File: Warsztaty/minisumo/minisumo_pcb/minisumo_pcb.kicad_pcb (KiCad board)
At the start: 2 copper layers, 100 x 100 mm, 49 parts, among them J1 HTSW-102-08-L-S, Q1 PMOS, U1 SN74LVC2G14DBV, U10 ITR8307-S17-TR8, U11 ITR8307-S17-TR8, U14 TB6612FNG, U2 TB6612FNG, U4 ATMEGA328P-AU, U7 LM1117S-5.0, U8 ITR8307-S17-TR8, Y1 ECS-160-20-4DN

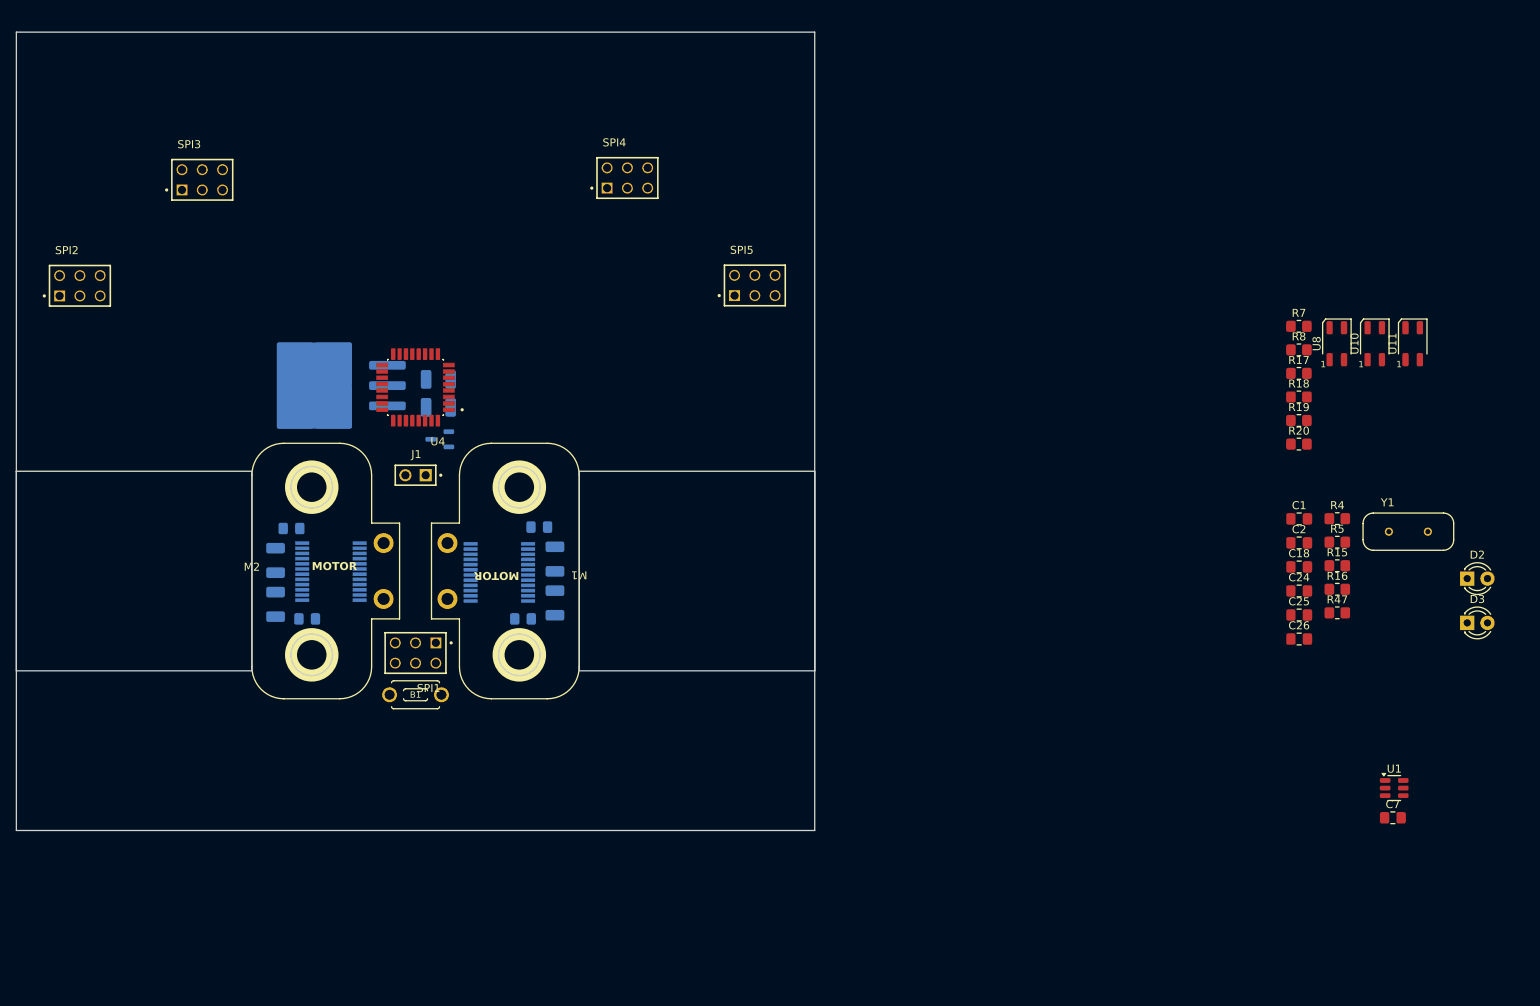
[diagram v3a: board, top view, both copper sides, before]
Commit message: Wstępny wyglad robota i płytki
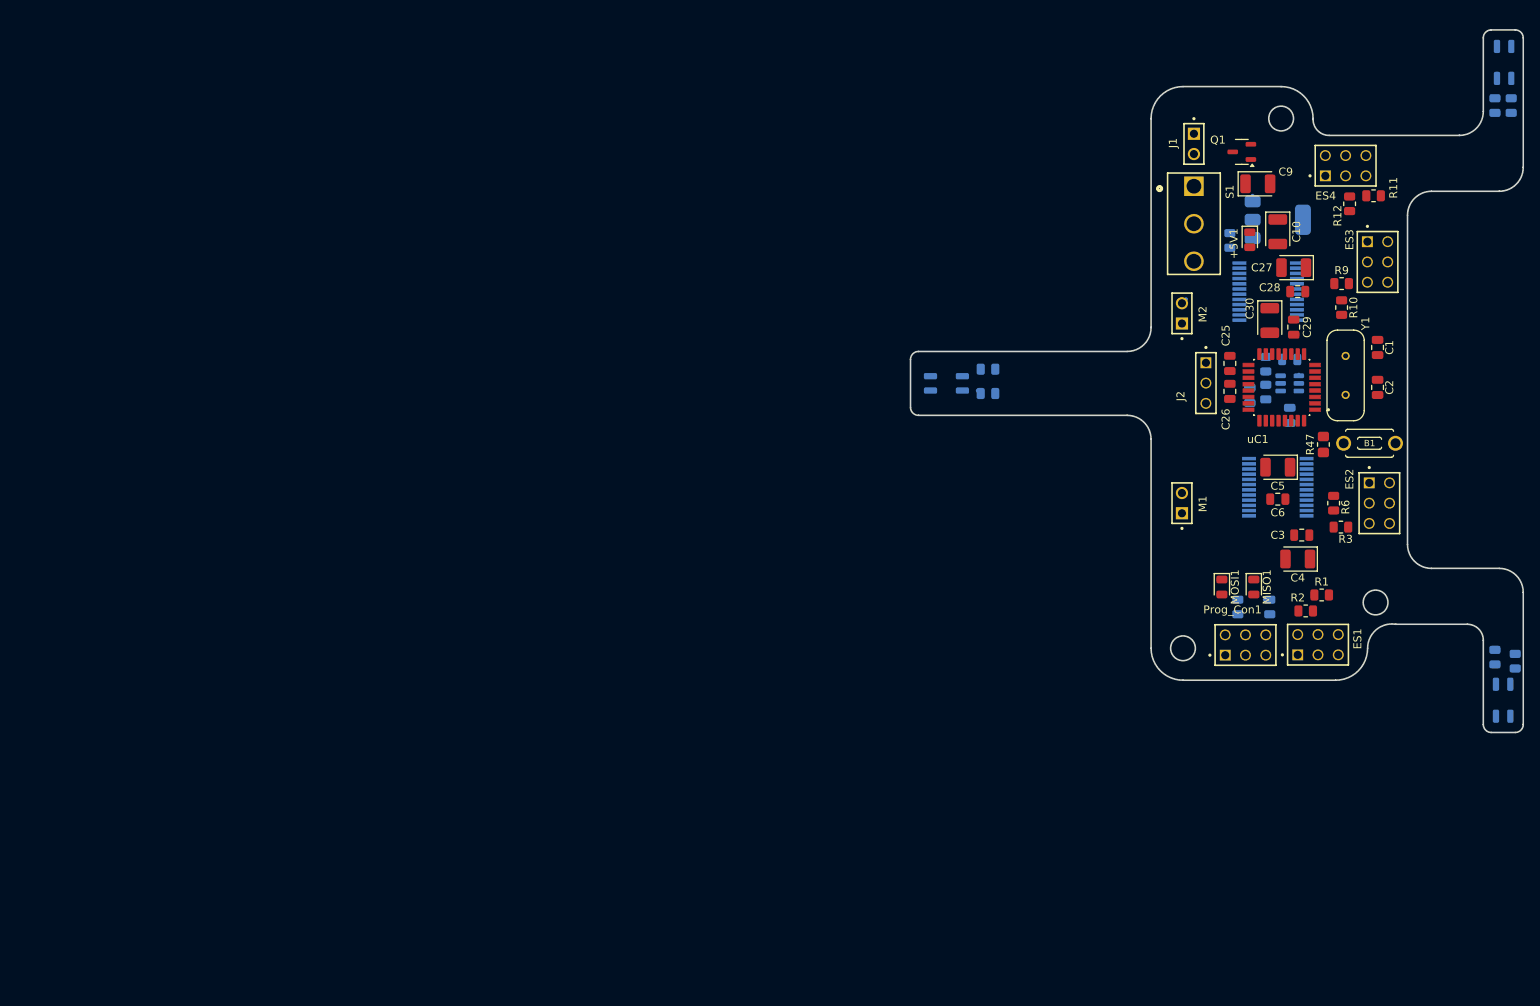
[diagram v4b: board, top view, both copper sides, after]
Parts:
- removed D2: red, LED_THT:LED_D3.0mm
- removed D3: green, LED_THT:LED_D3.0mm
- removed R18: 10k, Resistor_SMD:R_0805_2012Metric_Pad1.20x1.40mm_HandSolder
- removed SPI1, SPI2, SPI3, SPI4, SPI5: MTSW-103-23-F-D-230, MTSW-103-23-F-D-230:SAMTEC_MTSW-103-23-F-D-230
- removed U1: SN74LVC2G14DBV, Package_TO_SOT_SMD:SOT-23-6
- removed U10, U11, U8: ITR8307-S17-TR8, OptoDevice:Everlight_ITR1201SR10AR
- removed U14, U2: TB6612FNG, Package_SO:SSOP-24_5.3x8.2mm_P0.65mm
- removed U4: ATMEGA328P-AU, ATMEGA328P-AU:QFP80P900X900X120-32N
- added +5V1: green, LED_SMD:LED_0805_2012Metric, F.Cu at (204.5, 61.0)
- added ES1: MTSW-103-23-F-D-230, MTSW-103-23-F-D-230:SAMTEC_MTSW-103-23-F-D-230, F.Cu at (210.5, 113.0)
- added ES2: MTSW-103-23-F-D-230, MTSW-103-23-F-D-230:SAMTEC_MTSW-103-23-F-D-230, F.Cu at (219.5, 91.5)
- added ES3: MTSW-103-23-F-D-230, MTSW-103-23-F-D-230:SAMTEC_MTSW-103-23-F-D-230, F.Cu at (219.2, 61.2)
- added ES4: MTSW-103-23-F-D-230, MTSW-103-23-F-D-230:SAMTEC_MTSW-103-23-F-D-230, F.Cu at (214.0, 53.0)
- added INVERTER1: SN74LVC2G14DBV, Package_TO_SOT_SMD:SOT-23-6, B.Cu at (209.5, 79.0)
- added J2: MTSW-103-23-F-S-235, MTSW-103-23-F-S-235:SAMTEC_MTSW-103-23-F-S-235, F.Cu at (199.0, 79.0)
- added LS1: ITR8307-S17-TR8, OptoDevice:Everlight_ITR1201SR10AR, B.Cu at (236.2, 118.7)
- added LS2: ITR8307-S17-TR8, OptoDevice:Everlight_ITR1201SR10AR, B.Cu at (236.4, 38.8)
- added LS3: ITR8307-S17-TR8, OptoDevice:Everlight_ITR1201SR10AR, B.Cu at (166.5, 79.0)
- added MISO1: red, LED_SMD:LED_0805_2012Metric, F.Cu at (205.0, 104.5)
- added MOSI1: green, LED_SMD:LED_0805_2012Metric, F.Cu at (201.0, 104.5)
- added M_DRIVER1: TB6612FNG, Package_SO:SSOP-24_5.3x8.2mm_P0.65mm, B.Cu at (208.0, 92.0)
- added M_DRIVER2: TB6612FNG, Package_SO:SSOP-24_5.3x8.2mm_P0.65mm, B.Cu at (206.8, 67.5)
- added Prog_Con1: MTSW-103-23-F-D-230, MTSW-103-23-F-D-230:SAMTEC_MTSW-103-23-F-D-230, F.Cu at (201.4, 113.0)
- added R1: 10k, Resistor_SMD:R_0805_2012Metric, F.Cu at (213.5, 105.5)
- added R10: 10k, Resistor_SMD:R_0805_2012Metric, F.Cu at (216.0, 69.5)
- added R11: 20k, Resistor_SMD:R_0805_2012Metric, F.Cu at (220.0, 55.5)
- added R12: 10k, Resistor_SMD:R_0805_2012Metric, F.Cu at (217.0, 56.5)
- added R13: 200R, Resistor_SMD:R_0805_2012Metric, B.Cu at (171.7, 77.2)
- added R14: 10k, Resistor_SMD:R_0805_2012Metric, B.Cu at (171.7, 80.3)
- added R2: 20k, Resistor_SMD:R_0805_2012Metric, F.Cu at (211.5, 107.5)
- added R3: 20k, Resistor_SMD:R_0805_2012Metric, F.Cu at (215.9, 97.0)
- added R6: 10k, Resistor_SMD:R_0805_2012Metric, F.Cu at (215.0, 94.0)
- added R9: 20k, Resistor_SMD:R_0805_2012Metric, F.Cu at (216.0, 66.5)
- added S1: 1101M2S3CQE2, 1101M2S3CQE2:SW_1101M2S3CQE2, F.Cu at (197.5, 59.0)
- added uC1: ATMEGA328P-AU, ATMEGA328P-AU:QFP80P900X900X120-32N, F.Cu at (208.5, 79.5)
- C1, C2, C25, C26: footprint Capacitor_SMD:C_0805_2012Metric_Pad1.18x1.45mm_HandSolder -> Capacitor_SMD:C_0805_2012Metric
- C10, C27, C30, C4, C5, C9, Q1: moved to F.Cu
- C18, C24, C7: footprint Capacitor_SMD:C_0805_2012Metric_Pad1.18x1.45mm_HandSolder -> Capacitor_SMD:C_0805_2012Metric; moved to B.Cu
- C28, C29, C3, C6: value 10nF -> 100nF; footprint Capacitor_SMD:C_0805_2012Metric_Pad1.18x1.45mm_HandSolder -> Capacitor_SMD:C_0805_2012Metric; moved to F.Cu
- M1, M2: value ~ -> HTSW-102-08-L-S; footprint Motors_KoNaR:KoNaR_Motor -> HTSW-102-08-L-S:SAMTEC_HTSW-102-08-L-S
- R15, R16, R17, R19, R20, R8: footprint Resistor_SMD:R_0805_2012Metric_Pad1.20x1.40mm_HandSolder -> Resistor_SMD:R_0805_2012Metric; moved to B.Cu
- R4, R5: value 180 -> 1k; footprint Resistor_SMD:R_0805_2012Metric_Pad1.20x1.40mm_HandSolder -> Resistor_SMD:R_0805_2012Metric; moved to B.Cu
- R7: value 200R -> 180; footprint Resistor_SMD:R_0805_2012Metric_Pad1.20x1.40mm_HandSolder -> Resistor_SMD:R_0805_2012Metric; moved to B.Cu
- U7: footprint Package_TO_SOT_SMD:TO-263-3_TabPin2 -> Package_TO_SOT_SMD:SOT-223
- moved C4 128.0 mm to (210.5, 101.0), turned to 180 degrees
- moved C5 126.7 mm to (208.0, 89.5), turned to 180 degrees
- moved C3 126.5 mm to (211.0, 98.0), turned to 180 degrees
- moved B1 123.6 mm to (219.5, 86.5)
- moved C6 122.5 mm to (208.0, 93.5), turned to 180 degrees
- moved U7 121.0 mm to (208.0, 58.5), turned to 0 degrees
- moved M2 120.9 mm to (196.0, 70.2), turned to -90 degrees
- moved C10 106.8 mm to (208.0, 60.0), turned to -90 degrees
- moved Q1 106.7 mm to (203.5, 50.0)
- moved C9 106.4 mm to (205.5, 54.0)
- moved J1 106.0 mm to (197.5, 49.0), turned to 90 degrees
- moved C28 105.3 mm to (210.5, 67.5)
- moved C27 101.6 mm to (210.0, 64.5), turned to 180 degrees
- moved C29 97.8 mm to (210.0, 72.0), turned to -90 degrees
- moved C30 94.4 mm to (207.0, 71.1)
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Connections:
- R20 pad 1: /line_sensors/LS3 -> /line_sensors/LS1
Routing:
- net +BATT: track 0.00 -> 1.18 mm
- net +: track 0.00 -> 0.91 mm
- net /motor_driver2/MOTOR_IN2: track 0.00 -> 0.72 mm
- net Net-(uC1-AREF): track 0.00 -> 0.63 mm
- net Net-(MISO1-A): track 0.00 -> 0.62 mm
- net Net-(ES3-Pad05): track 0.00 -> 0.58 mm
- net /line_sensors/LS3: track 0.00 -> 0.51 mm
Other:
- board size 100 x 100 mm -> 76.7 x 88 mm

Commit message: koncowy projekt plytki i chyba model tez
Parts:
- removed J1: HTSW-102-08-L-S, HTSW-102-08-L-S:SAMTEC_HTSW-102-08-L-S
- added BATT1: HTSW-102-08-L-S, HTSW-102-08-L-S:SAMTEC_HTSW-102-08-L-S, F.Cu at (138.0, 74.5)
- C1, C10, C2, C25, C26, C9: moved to B.Cu
- C18, R15, R16, R4, R5: moved to F.Cu
- moved LS1 127.8 mm to (111.5, 91.0), turned to 90 degrees
- moved R20 123.3 mm to (117.0, 88.9), turned to -90 degrees
- moved R17 119.9 mm to (117.0, 93.0), turned to 180 degrees
- moved R11 101.7 mm to (153.0, 132.0), turned to 0 degrees
- moved R12 97.1 mm to (153.0, 129.5), turned to 180 degrees
- moved ES4 92.7 mm to (161.5, 129.5), turned to 180 degrees
- moved B1 90.1 mm to (129.5, 91.0), turned to 0 degrees
- moved C27 74.5 mm to (154.6, 114.4), turned to 45 degrees
- moved C28 73.4 mm to (150.0, 109.0)
- moved M_DRIVER2 73.3 mm to (152.6, 116.9), turned to -90 degrees
- moved ES1 70.7 mm to (158.7, 64.8)
- moved C1 70.7 mm to (151.7, 90.7), turned to 45 degrees
- moved ES3 68.8 mm to (164.7, 103.2)
- moved Prog_Con1 68.4 mm to (137.0, 90.1), turned to 45 degrees
- moved C29 68.3 mm to (160.0, 118.5)
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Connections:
- Q1 pad 1: + -> +OUT
- S1 pad 1: + -> +OUT
- S1 pad 2: + -> +IN
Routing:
- net GND: track 0.00 -> 375.1 mm, vias 0 -> 23
- net +5V: track 0.39 -> 313.4 mm, vias 0 -> 14
- net +BATT: track 1.18 -> 131.8 mm, vias 0 -> 10
- net /sensor1/SCL: track 0.00 -> 96.6 mm, vias 0 -> 4
- net /sensor1/SDA: track 0.00 -> 90.6 mm, vias 0 -> 2
- net /inverter/DIRB_2: track 0.00 -> 69.6 mm, vias 0 -> 2
- net /line_sensors/LS2: track 0.00 -> 67.0 mm, vias 0 -> 1
- net /line_sensors/LS1: track 0.00 -> 56.1 mm, vias 0 -> 1
- net /line_sensors/LS3: track 0.51 -> 53.7 mm, vias 0 -> 3
- net /inverter/DIRA_2: track 0.14 -> 44.8 mm, vias 0 -> 2
- net /sensor1/X1: track 0.00 -> 42.3 mm, vias 0 -> 2
- net /motor_driver2/PWM2: track 0.00 -> 37.9 mm, vias 0 -> 1
- net /sensor4/X4: track 0.00 -> 36.6 mm
- net /programming_connector/RST: track 0.00 -> 35.2 mm, vias 0 -> 1
- net /inverter/DIRB_1: track 0.00 -> 28.4 mm, vias 0 -> 2
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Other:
- outline, holes or cut-outs redrawn
- board text added: "MEFON V1.0 minisumo ADAM PRYSTUPA"

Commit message: prawdopodobnie koncowa wersja płytki
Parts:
- C1, C2, C24, C25, C26: moved to F.Cu
- C18, C27, C28, C29, C3, C30, C4, C5, C6, Q1: moved to B.Cu
- moved R47 36.1 mm to (118.7, 98.4), turned to 45 degrees
- moved C18 34.7 mm to (122.1, 98.0), turned to 45 degrees
- moved R14 34.4 mm to (148.6, 138.4), turned to 0 degrees
- moved Q1 33.0 mm to (119.2, 69.3), turned to -90 degrees
- moved +5V1 32.9 mm to (119.6, 85.3)
- moved R13 31.7 mm to (152.6, 136.2), turned to 0 degrees
- moved C28 31.2 mm to (127.6, 130.8), turned to -135 degrees
- moved C27 31.1 mm to (129.7, 133.0), turned to -135 degrees
- moved R7 30.9 mm to (122.1, 82.8)
- moved C9 30.7 mm to (119.5, 75.2), turned to 180 degrees
- moved R11 30.4 mm to (124.7, 143.2)
- moved R12 30.4 mm to (124.7, 140.7)
- moved B1 30.4 mm to (101.2, 102.2)
- moved BATT1 30.4 mm to (109.7, 85.7)
- moved J2 30.4 mm to (110.2, 119.2)
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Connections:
- R1 pad 2: /sensor1/X1 -> /sensor1/XSHUT_1
- R10 pad 2: /sensor3/X3 -> /sensor3/XSHUT_3
- R12 pad 2: /sensor4/X4 -> /sensor4/XSHUT_4
- R6 pad 2: /sensor2/X2 -> /sensor2/XSHUT_2
- uC1 pad 1: /sensor4/X4 -> /sensor1/XSHUT_1
- uC1 pad 10: /motor_driver2/PWM2 -> unconnected-(uC1-PD6-Pad10)
- uC1 pad 11: /inverter/DIRB_2 -> unconnected-(uC1-PD7-Pad11)
- uC1 pad 12: unconnected-(uC1-PB0-Pad12) -> /inverter/DIRB_2
- uC1 pad 13: unconnected-(uC1-PB1-Pad13) -> /motor_driver1/PWM1
- uC1 pad 14: unconnected-(uC1-PB2-Pad14) -> /motor_driver2/PWM2
- uC1 pad 23: /line_sensors/LS3 -> /line_sensors/LS1
- uC1 pad 24: /line_sensors/LS2 -> /line_sensors/LS3
- uC1 pad 25: /line_sensors/LS1 -> /line_sensors/LS2
- uC1 pad 30: /sensor1/X1 -> /sensor4/XSHUT_4
- uC1 pad 31: /sensor2/X2 -> /sensor3/XSHUT_3
- uC1 pad 32: /sensor3/X3 -> /sensor2/XSHUT_2
- uC1 pad 9: /motor_driver1/PWM1 -> unconnected-(uC1-PD5-Pad9)
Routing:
- net GND: track 375.1 -> 47.2 mm, vias 23 -> 486
- net /sensor4/XSHUT_4: track 0.00 -> 44.6 mm, vias 0 -> 2
- net /sensor2/XSHUT_2: track 0.00 -> 42.8 mm, vias 0 -> 4
- net /sensor1/X1: track 42.3 -> 0.00 mm, vias 2 -> 0
- net /sensor4/X4: track 36.6 -> 0.00 mm
- net /sensor1/XSHUT_1: track 0.00 -> 35.9 mm
- net /sensor1/SDA: track 90.6 -> 119.7 mm, vias 2 -> 3
- net /sensor1/SCL: track 96.6 -> 119.7 mm, vias 4 -> 2
- net +BATT: track 131.8 -> 153.2 mm, vias 10 -> 1
- net /sensor2/X2: track 20.4 -> 0.00 mm, vias 2 -> 0
- net /sensor3/XSHUT_3: track 0.00 -> 20.1 mm
- net /sensor3/X3: track 18.8 -> 0.00 mm, vias 2 -> 0
- net /programming_connector/RST: track 35.2 -> 53.9 mm, vias 1 -> 2
- net STARTER: track 14.4 -> 27.5 mm
- net /motor_driver2/PWM2: track 37.9 -> 50.3 mm, vias 1 -> 3
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- added copper zone on B.Cu, net GND
- added copper zone on F.Cu, net GND
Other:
- outline, holes or cut-outs redrawn

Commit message: ostateczna wersja plytki
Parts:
- moved R6 2.47 mm to (140.6, 73.0)
- moved R3 2.20 mm to (140.6, 75.6)
- moved ES2 2.19 mm to (149.6, 73.0)
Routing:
- net /sensor1/SCL: track 119.7 -> 116.5 mm
- net /sensor1/SDA: track 119.7 -> 116.9 mm
- net Net-(ES2-Pad05): track 7.14 -> 6.08 mm
- net +5V: track 309.7 -> 310.6 mm
- net /line_sensors/LS2: track 58.1 -> 58.9 mm
- net GND: vias 486 -> 902

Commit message: wersja ostateczna plytki - gotowe gerbery do zamowienia
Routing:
- net +5V: track 310.6 -> 312.1 mm
- net /sensor1/SDA: track 116.9 -> 117.5 mm
- net /inverter/DIRB_1: track 34.8 -> 34.3 mm
- net GND: vias 902 -> 894
